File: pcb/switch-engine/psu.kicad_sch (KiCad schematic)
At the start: 122 parts, among them J1 CONN_PCIE_PWR_8PIN, J2 CONN_IBC_MGMT, J3 CONN_01X03, J4 CORTEX_DEBUG_ETM, J5 FAN_01, J6 FAN_01, SW1 SWITCH, SW2 SWITCH, U1 STM32L431-QFN48, U2 MYMGK1R812ERSR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

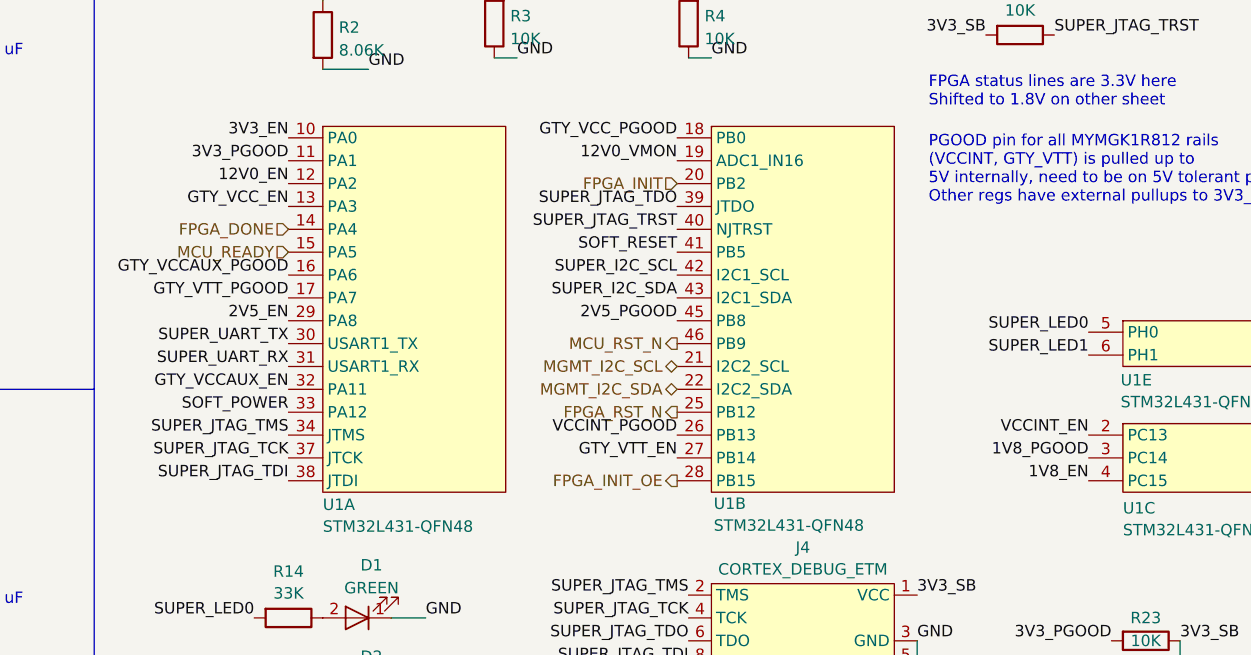
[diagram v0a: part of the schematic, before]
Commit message: Started routing supervisor area in northeast corner
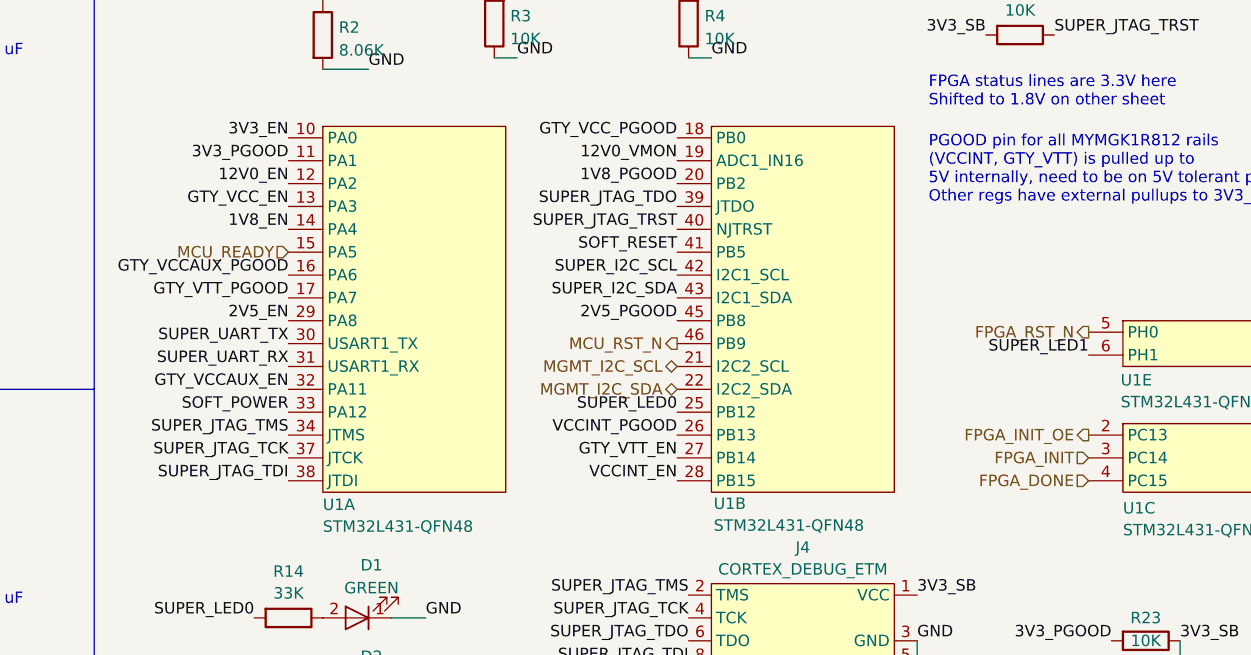
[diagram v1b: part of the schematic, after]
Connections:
- net 1V8_EN: now also U1.14 (PA4); no longer U1.4 (PC15)
- net 1V8_PGOOD: now also U1.20 (PB2); no longer U1.3 (PC14)
- net FPGA_DONE: now also U1.4 (PC15); no longer U1.14 (PA4)
- net FPGA_INIT: now also U1.3 (PC14); no longer U1.20 (PB2)
- net FPGA_INIT_OE: now also U1.2 (PC13); no longer U1.28 (PB15)
- net FPGA_RST_N: now also U1.5 (PH0); no longer U1.25 (PB12)
- net SUPER_LED0: now also U1.25 (PB12); no longer U1.5 (PH0)
- net VCCINT_EN: now also U1.28 (PB15); no longer U1.2 (PC13)
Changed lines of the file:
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@@
 	)
 	(label "1V8_PGOOD"
-		(at 375.92 135.89 180)
+		(at 330.2 105.41 180)
 		(fields_autoplaced yes)
 		(effects
@@
 	)
 	(label "VCCINT_EN"
-		(at 375.92 133.35 180)
+		(at 330.2 138.43 180)
 		(fields_autoplaced yes)
 		(effects
@@
 	)
 	(label "1V8_EN"
-		(at 375.92 138.43 180)
+		(at 287.02 110.49 180)
 		(fields_autoplaced yes)
 		(effects
@@
 	)
 	(label "SUPER_LED0"
-		(at 375.92 121.92 180)
+		(at 330.2 130.81 180)
 		(fields_autoplaced yes)
 		(effects
@@
 	(hierarchical_label "FPGA_INIT"
 		(shape input)
-		(at 330.2 105.41 180)
+		(at 375.92 135.89 180)
 		(fields_autoplaced yes)
 		(effects
@@
 	(hierarchical_label "FPGA_DONE"
 		(shape input)
-		(at 287.02 110.49 180)
+		(at 375.92 138.43 180)
 		(fields_autoplaced yes)
 		(effects
@@
 	(hierarchical_label "FPGA_RST_N"
 		(shape output)
-		(at 330.2 130.81 180)
+		(at 375.92 121.92 180)
 		(fields_autoplaced yes)
 		(effects
@@
 	(hierarchical_label "FPGA_INIT_OE"
 		(shape output)
-		(at 330.2 138.43 180)
-		(fields_autoplaced yes)
-		(effects
+		(at 375.92 133.35 180)
+		(fields_autoplaced yes)
+		(effects

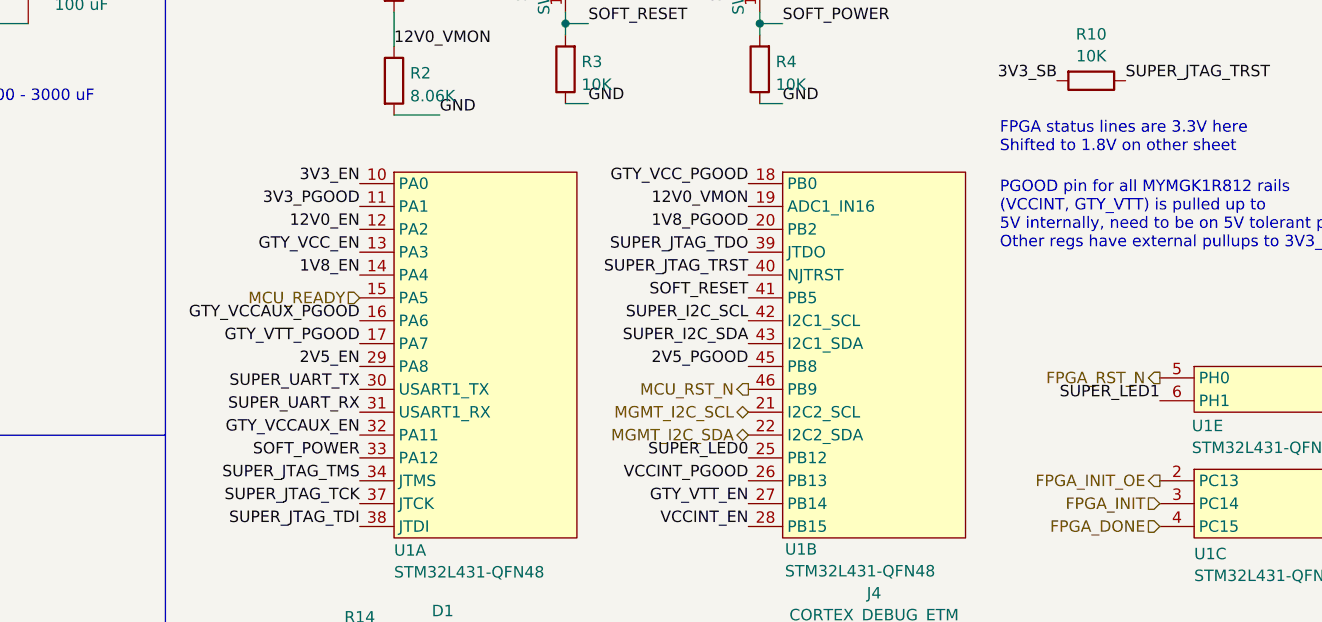
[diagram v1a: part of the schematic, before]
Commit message: More work on supervisor area
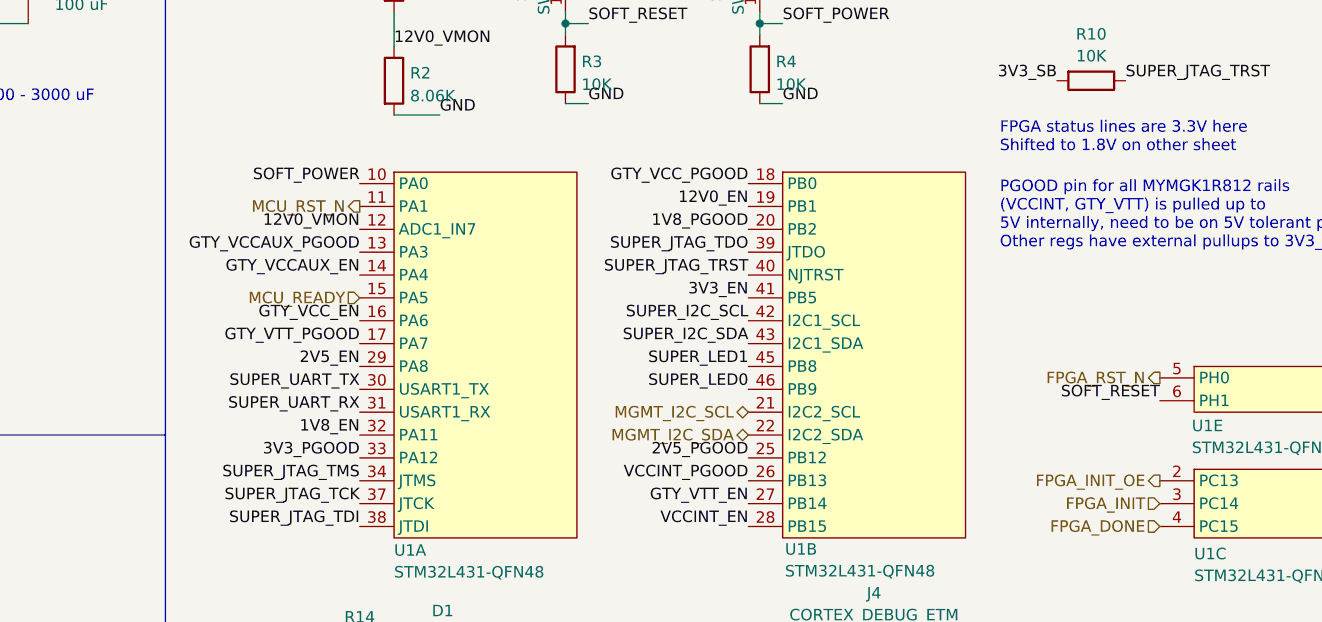
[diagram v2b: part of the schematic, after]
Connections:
- net 12V0_EN: now also U1.19 (PB1); no longer U1.12 (PA2)
- net 12V0_VMON: now also U1.12 (PA2); no longer U1.19 (PB1)
- net 1V8_EN: now also U1.32 (PA11); no longer U1.14 (PA4)
- net 2V5_PGOOD: now also U1.25 (PB12); no longer U1.45 (PB8)
- net 3V3_EN: now also U1.41 (PB5); no longer U1.10 (PA0)
- net 3V3_PGOOD: now also U1.33 (PA12); no longer U1.11 (PA1)
- net GTY_VCCAUX_EN: now also U1.14 (PA4); no longer U1.32 (PA11)
- net GTY_VCCAUX_PGOOD: now also U1.13 (PA3); no longer U1.16 (PA6)
- net GTY_VCC_EN: now also U1.16 (PA6); no longer U1.13 (PA3)
- net MCU_RST_N: now also U1.11 (PA1); no longer U1.46 (PB9)
- net SOFT_POWER: now also U1.10 (PA0); no longer U1.33 (PA12)
- net SOFT_RESET: now also U1.6 (PH1); no longer U1.41 (PB5)
- net SUPER_LED0: now also U1.46 (PB9); no longer U1.25 (PB12)
- net SUPER_LED1: now also U1.45 (PB8); no longer U1.6 (PH1)
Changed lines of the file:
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@@
 	)
 	(label "GTY_VCCAUX_EN"
-		(at 287.02 128.27 180)
+		(at 287.02 110.49 180)
 		(fields_autoplaced yes)
 		(effects
@@
 	)
 	(label "12V0_EN"
-		(at 287.02 105.41 180)
+		(at 330.2 102.87 180)
 		(fields_autoplaced yes)
 		(effects
@@
 	)
 	(label "3V3_PGOOD"
-		(at 287.02 102.87 180)
+		(at 287.02 130.81 180)
 		(fields_autoplaced yes)
 		(effects
@@
 	)
 	(label "3V3_EN"
-		(at 287.02 100.33 180)
+		(at 330.2 113.03 180)
 		(fields_autoplaced yes)
 		(effects
@@
 	)
 	(label "SUPER_LED1"
-		(at 375.92 124.46 180)
+		(at 330.2 120.65 180)
 		(fields_autoplaced yes)
 		(effects
@@
 	)
 	(label "GTY_VCCAUX_PGOOD"
-		(at 287.02 115.57 180)
+		(at 287.02 107.95 180)
 		(fields_autoplaced yes)
 		(effects
@@
 	)
 	(label "12V0_VMON"
-		(at 330.2 102.87 180)
+		(at 287.02 105.41 180)
 		(fields_autoplaced yes)
 		(effects
@@
 	)
 	(label "SOFT_POWER"
-		(at 287.02 130.81 180)
+		(at 287.02 100.33 180)
 		(fields_autoplaced yes)
 		(effects
@@
 	)
 	(label "1V8_EN"
-		(at 287.02 110.49 180)
+		(at 287.02 128.27 180)
 		(fields_autoplaced yes)
 		(effects
@@
 	)
 	(label "SUPER_LED0"
-		(at 330.2 130.81 180)
+		(at 330.2 123.19 180)
 		(fields_autoplaced yes)
 		(effects
@@
 	)
 	(label "SOFT_RESET"
-		(at 330.2 113.03 180)
+		(at 375.92 124.46 180)
 		(fields_autoplaced yes)
 		(effects
@@
 	)
 	(label "2V5_PGOOD"
-		(at 330.2 120.65 180)
+		(at 330.2 130.81 180)
 		(fields_autoplaced yes)
 		(effects
@@
 	)
 	(label "GTY_VCC_EN"
-		(at 287.02 107.95 180)
+		(at 287.02 115.57 180)
 		(fields_autoplaced yes)
 		(effects
@@
 	(hierarchical_label "MCU_RST_N"
 		(shape output)
-		(at 330.2 123.19 180)
+		(at 287.02 102.87 180)
 		(fields_autoplaced yes)
 		(effects
@@
 		)
 		(pin "12"
+			(alternate "ADC1_IN7")
 		)
 		(pin "34"
@@
 		)
 		(pin "19"
-			(alternate "ADC1_IN16")
 		)
 		(pin "13"
@@
 		)
 		(pin "12"
+			(alternate "ADC1_IN7")
 		)
 		(pin "34"
@@
 		)
 		(pin "19"
-			(alternate "ADC1_IN16")
 		)
 		(pin "13"
@@
 		)
 		(pin "12"
+			(alternate "ADC1_IN7")
 		)
 		(pin "34"
@@
 		)
 		(pin "19"
-			(alternate "ADC1_IN16")
 		)
 		(pin "13"
@@
 		)
 		(pin "12"
+			(alternate "ADC1_IN7")
 		)
 		(pin "34"
@@
 		)
 		(pin "19"
-			(alternate "ADC1_IN16")
 		)
 		(pin "13"
@@
 		)
 		(pin "12"
+			(alternate "ADC1_IN7")
 		)
 		(pin "34"
@@
 		)
 		(pin "19"
-			(alternate "ADC1_IN16")
 		)
 		(pin "13"

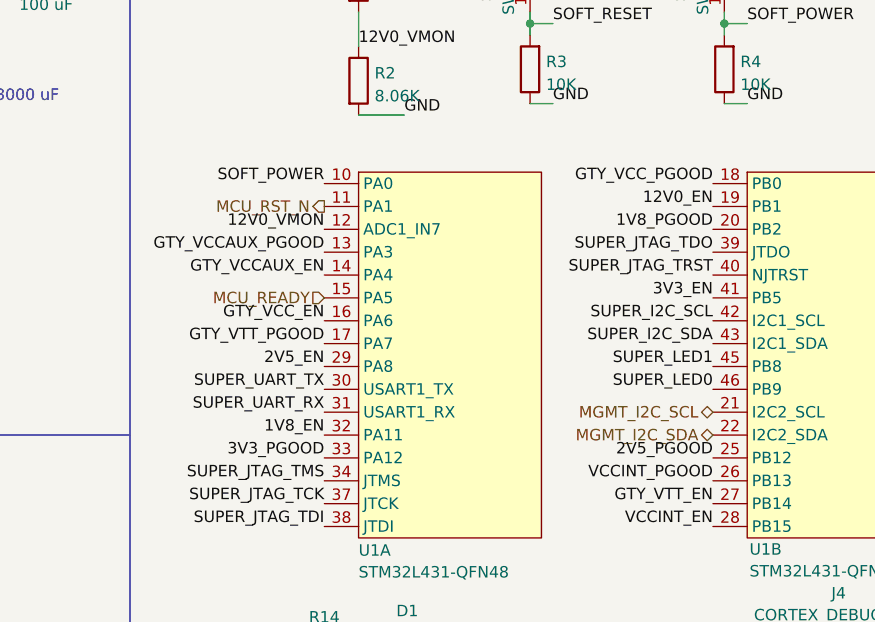
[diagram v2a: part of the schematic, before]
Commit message: Continued right side layout, basically everything done except power supply
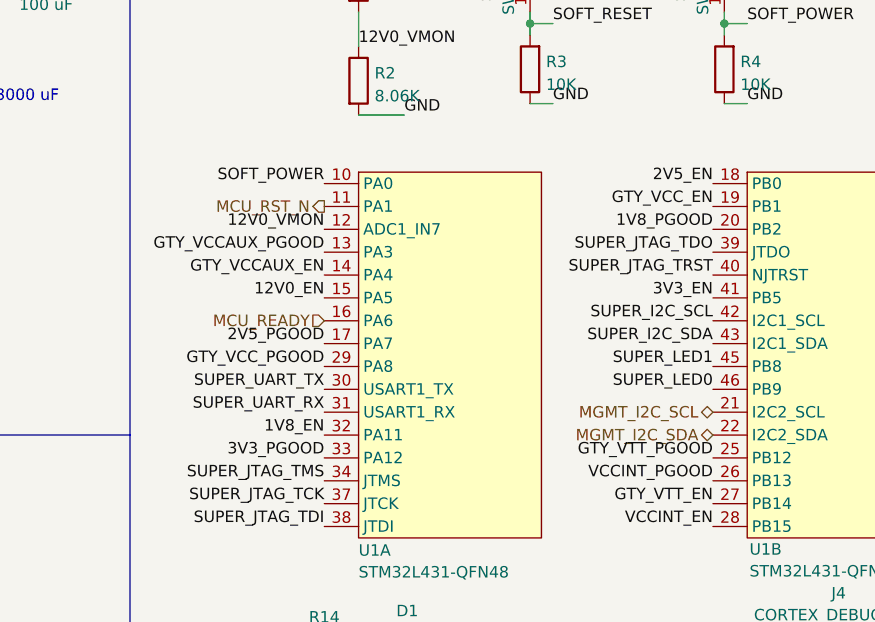
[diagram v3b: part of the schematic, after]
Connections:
- net 12V0_EN: now also U1.15 (PA5); no longer U1.19 (PB1)
- net 2V5_EN: now also U1.18 (PB0); no longer U1.29 (PA8)
- net 2V5_PGOOD: now also U1.17 (PA7); no longer U1.25 (PB12)
- net GTY_VCC_EN: now also U1.19 (PB1); no longer U1.16 (PA6)
- net GTY_VCC_PGOOD: now also U1.29 (PA8); no longer U1.18 (PB0)
- net GTY_VTT_PGOOD: now also U1.25 (PB12); no longer U1.17 (PA7)
- net MCU_READY: now also U1.16 (PA6); no longer U1.15 (PA5)
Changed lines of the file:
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@@
 	)
 	(label "12V0_EN"
-		(at 330.2 102.87 180)
+		(at 287.02 113.03 180)
 		(fields_autoplaced yes)
 		(effects
@@
 	)
 	(label "GTY_VCC_PGOOD"
-		(at 330.2 100.33 180)
+		(at 287.02 120.65 180)
 		(fields_autoplaced yes)
 		(effects
@@
 	)
 	(label "GTY_VTT_PGOOD"
-		(at 287.02 118.11 180)
+		(at 330.2 130.81 180)
 		(fields_autoplaced yes)
 		(effects
@@
 	)
 	(label "2V5_EN"
-		(at 287.02 120.65 180)
+		(at 330.2 100.33 180)
 		(fields_autoplaced yes)
 		(effects
@@
 	)
 	(label "2V5_PGOOD"
-		(at 330.2 130.81 180)
+		(at 287.02 118.11 180)
 		(fields_autoplaced yes)
 		(effects
@@
 	)
 	(label "GTY_VCC_EN"
-		(at 287.02 115.57 180)
+		(at 330.2 102.87 180)
 		(fields_autoplaced yes)
 		(effects
@@
 	(hierarchical_label "MCU_READY"
 		(shape input)
-		(at 287.02 113.03 180)
-		(fields_autoplaced yes)
-		(effects
+		(at 287.02 115.57 180)
+		(fields_autoplaced yes)
+		(effects

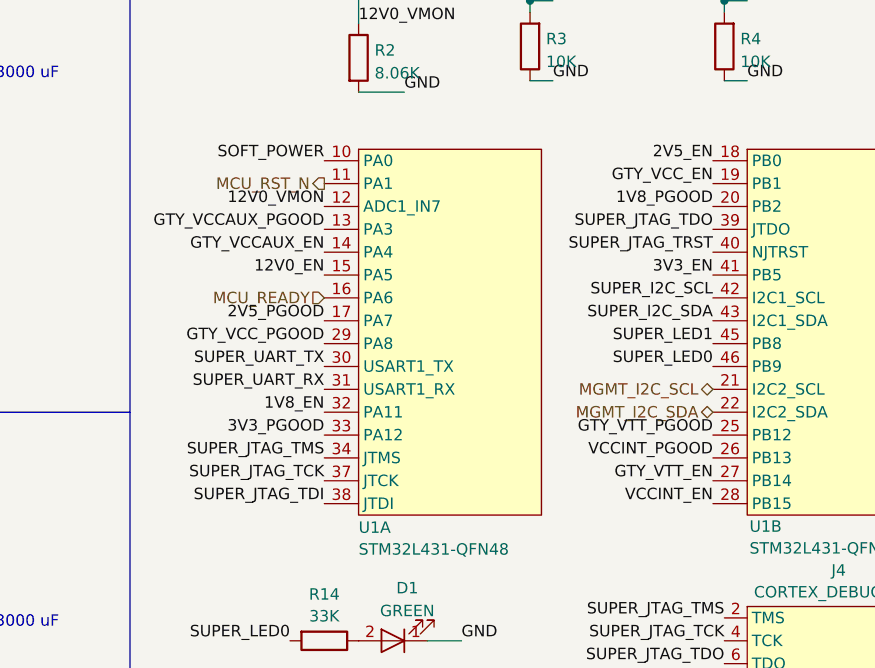
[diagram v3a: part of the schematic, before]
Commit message: Updating file: switch-engine.kicad_pcb with current completely routed design
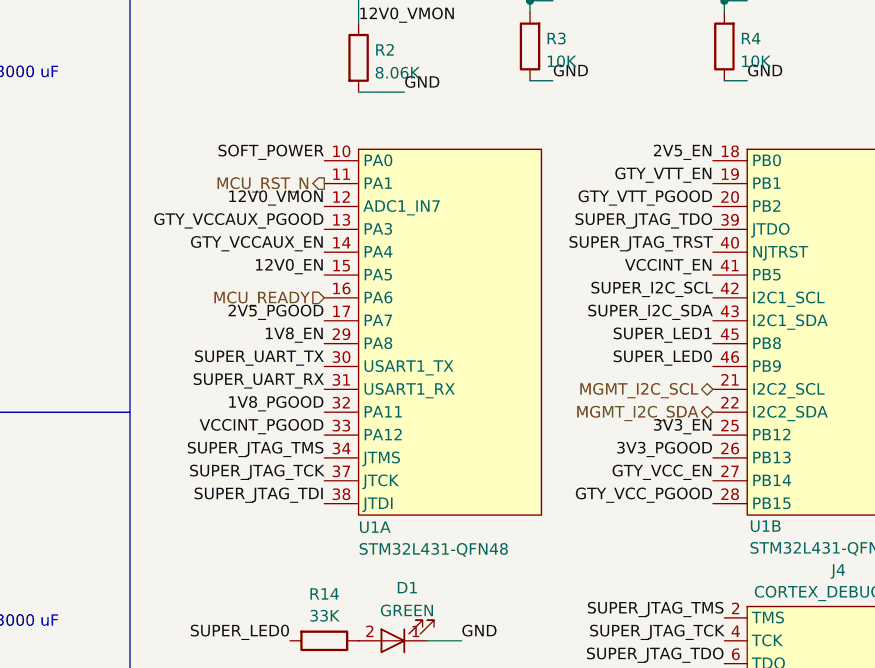
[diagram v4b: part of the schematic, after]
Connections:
- net 1V8_EN: now also U1.29 (PA8); no longer U1.32 (PA11)
- net 1V8_PGOOD: now also U1.32 (PA11); no longer U1.20 (PB2)
- net 3V3_EN: now also U1.25 (PB12); no longer U1.41 (PB5)
- net 3V3_PGOOD: now also U1.26 (PB13); no longer U1.33 (PA12)
- net GTY_VCC_EN: now also U1.27 (PB14); no longer U1.19 (PB1)
- net GTY_VCC_PGOOD: now also U1.28 (PB15); no longer U1.29 (PA8)
- net GTY_VTT_EN: now also U1.19 (PB1); no longer U1.27 (PB14)
- net GTY_VTT_PGOOD: now also U1.20 (PB2); no longer U1.25 (PB12)
- net VCCINT_EN: now also U1.41 (PB5); no longer U1.28 (PB15)
- net VCCINT_PGOOD: now also U1.33 (PA12); no longer U1.26 (PB13)
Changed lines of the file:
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@@
 	)
 	(label "3V3_PGOOD"
-		(at 287.02 130.81 180)
+		(at 330.2 133.35 180)
 		(fields_autoplaced yes)
 		(effects
@@
 	)
 	(label "1V8_PGOOD"
-		(at 330.2 105.41 180)
+		(at 287.02 128.27 180)
 		(fields_autoplaced yes)
 		(effects
@@
 	)
 	(label "VCCINT_EN"
-		(at 330.2 138.43 180)
+		(at 330.2 113.03 180)
 		(fields_autoplaced yes)
 		(effects
@@
 	)
 	(label "3V3_EN"
-		(at 330.2 113.03 180)
+		(at 330.2 130.81 180)
 		(fields_autoplaced yes)
 		(effects
@@
 	)
 	(label "GTY_VTT_EN"
-		(at 330.2 135.89 180)
+		(at 330.2 102.87 180)
 		(fields_autoplaced yes)
 		(effects
@@
 	)
 	(label "GTY_VCC_PGOOD"
-		(at 287.02 120.65 180)
+		(at 330.2 138.43 180)
 		(fields_autoplaced yes)
 		(effects
@@
 	)
 	(label "1V8_EN"
-		(at 287.02 128.27 180)
+		(at 287.02 120.65 180)
 		(fields_autoplaced yes)
 		(effects
@@
 	)
 	(label "GTY_VTT_PGOOD"
-		(at 330.2 130.81 180)
+		(at 330.2 105.41 180)
 		(fields_autoplaced yes)
 		(effects
@@
 	)
 	(label "GTY_VCC_EN"
-		(at 330.2 102.87 180)
+		(at 330.2 135.89 180)
 		(fields_autoplaced yes)
 		(effects
@@
 	)
 	(label "VCCINT_PGOOD"
-		(at 330.2 133.35 180)
-		(fields_autoplaced yes)
-		(effects
+		(at 287.02 130.81 180)
+		(fields_autoplaced yes)
+		(effects
